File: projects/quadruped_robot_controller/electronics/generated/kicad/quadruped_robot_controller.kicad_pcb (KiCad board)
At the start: 4 copper layers, 160 x 100 mm, 42 parts, among them J1 24V INPUT, J11 MOTOR_IO_1, J12 MOTOR_IO_2, J13 MOTOR_IO_3, J14 MOTOR_IO_4, J15 MOTOR_IO_5, J16 MOTOR_IO_6, J17 MOTOR_IO_7, J18 MOTOR_IO_8, J19 MOTOR_IO_9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

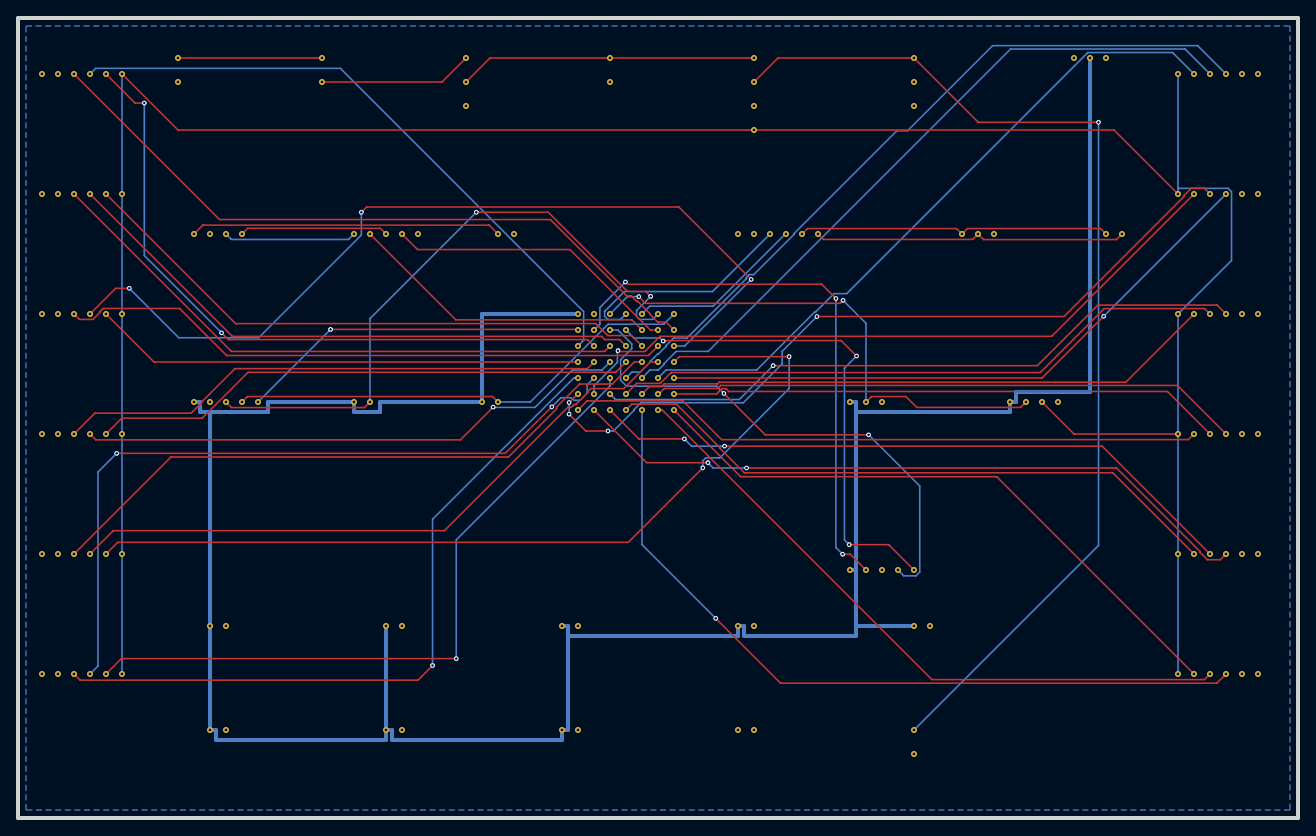
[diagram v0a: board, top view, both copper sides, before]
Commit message: feat: component resolver, provenance tracking, and tscircuit backend gate
- Add ComponentResolver and artifact_provenance to wire real component
  data (MPN, footprint, lifecycle) into the electrical graph
- Introduce TSCircuitBackend as the first release-eligible compiled
  electronics backend; reference backend now explicitly blocks release
- Move electronics design intent from .ato source files to annotated
  .intent.md files under electronics/intent/
- Reroute BOM to electronics/generated/bom.csv; release directory is
  now exports/releases/<revision> with atomic staging via .staging/
- Add candidate bundle writing per design iteration
- Normalise MCP tool status strings and rename generate_electronics to
  hw_generate_electronics_source / hw_generate_all
- Update all tests to reflect new gate names and blocked-by-default
  release policy for the reference backend
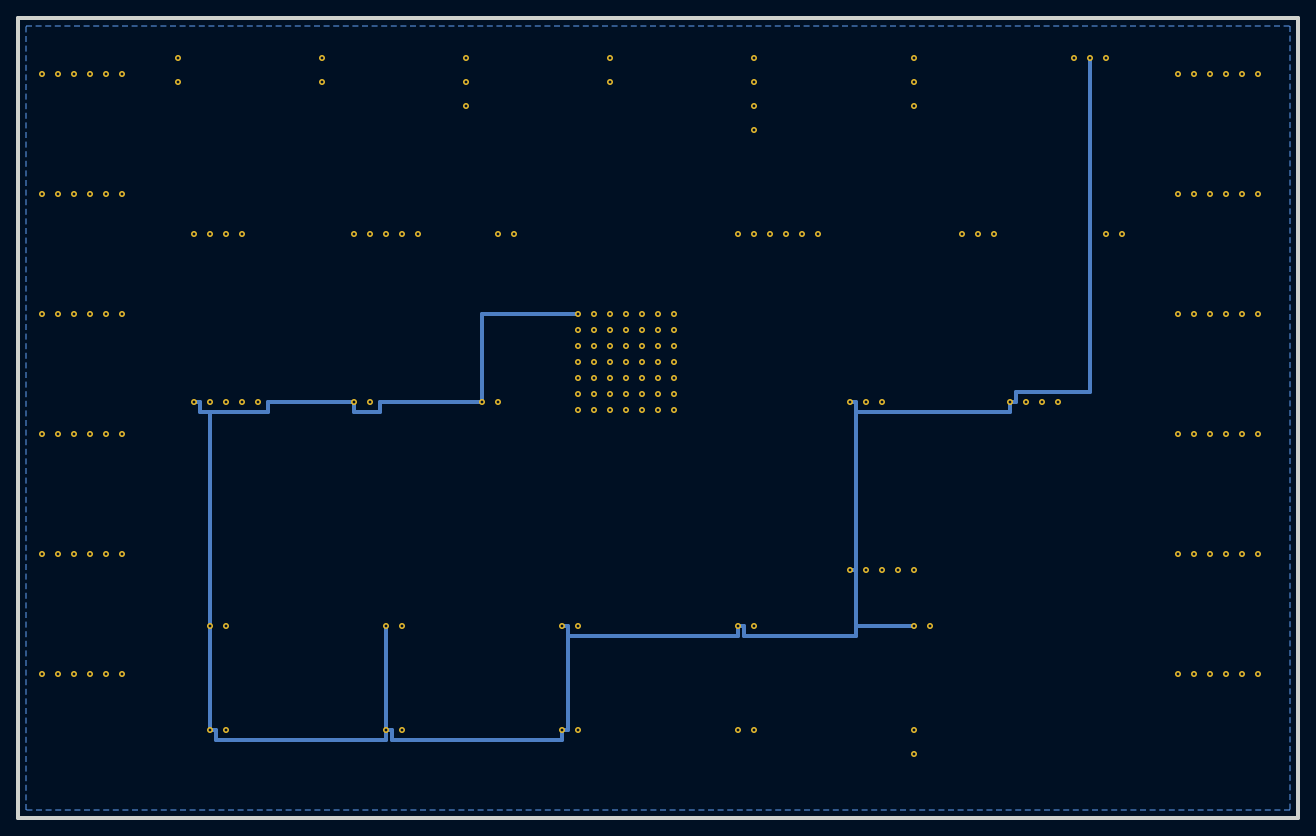
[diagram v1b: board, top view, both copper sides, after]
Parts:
- C1, C2, C3, C4, C5, C6, C7, C8: footprint C0603 -> Capacitor_SMD:C_0603_1608Metric
- C10: footprint C1210 -> Capacitor_SMD:C_1210_3225Metric
- C9: footprint C1206 -> Capacitor_SMD:C_1206_3216Metric
- D1: footprint SMCJ -> Diode_SMD:D_SMC
- D2, Q1, Q2: footprint SOT23-6 -> Package_TO_SOT_SMD:SOT-23-6
- F1: footprint MIDI_Fuse -> HW_Curated:MIDI_Fuse
- J1: footprint MicroFit_2Pin -> HW_Curated:MicroFit_2Pin
- J11, J12, J13, J14, J15, J16, J17, J18, J19, J20, J21, J22: footprint MicroFit_8Pin -> HW_Curated:MicroFit_8Pin
- J2: footprint Terminal_3Pin -> TerminalBlock:Phoenix_3Pin
- J3: footprint MicroFit_3Pin -> HW_Curated:MicroFit_3Pin
- J4: footprint Cortex_Debug_10Pin -> Connector_Samtec:FTSH-105
- J5: footprint USB_C_16Pin -> Connector_USB:USB_C_GCT_USB4105
- R1, R2, R3, R4: footprint R0603 -> Resistor_SMD:R_0603_1608Metric
- U1: footprint LQFP100 -> Package_QFP:LQFP-100_14x14mm_P0.5mm
- U2: footprint LGA14 -> Package_LGA:LGA-14
- U3: footprint VQFN24 -> Package_DFN_QFN:VQFN-24-1EP
- U4: footprint WQFN30 -> Package_DFN_QFN:WQFN-30
- U5: footprint VQFN16 -> Package_DFN_QFN:VQFN-16
- U6: footprint SOIC8 -> Package_SO:SOIC-8_3.9x4.9mm_P1.27mm
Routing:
- net ESTOP_GATE: track 316.8 -> 0.00 mm
- net VSYS: track 133.2 -> 0.00 mm, vias 1 -> 0
- net MOTOR5_ENC: track 113.1 -> 0.00 mm, vias 2 -> 0
- net MOTOR3_CURRENT: track 111.8 -> 0.00 mm, vias 3 -> 0
- net MOTOR8_CURRENT: track 97.9 -> 0.00 mm, vias 4 -> 0
- net MOTOR12_PWM: track 97.5 -> 0.00 mm, vias 1 -> 0
- net MOTOR7_PWM: track 93.9 -> 0.00 mm
- net MOTOR6_CURRENT: track 93.4 -> 0.00 mm, vias 2 -> 0
- net MOTOR6_PWM: track 89.7 -> 0.00 mm, vias 1 -> 0
- net MOTOR7_CURRENT: track 89.4 -> 0.00 mm
- net MOTOR1_PWM: track 88.3 -> 0.00 mm
- net MOTOR6_ENC: track 87.6 -> 0.00 mm, vias 1 -> 0
- net MOTOR11_PWM: track 87.1 -> 0.00 mm, vias 2 -> 0
- net MOTOR8_ENC: track 86.9 -> 0.00 mm, vias 1 -> 0
- net MOTOR1_ENC: track 86.2 -> 0.00 mm, vias 2 -> 0
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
